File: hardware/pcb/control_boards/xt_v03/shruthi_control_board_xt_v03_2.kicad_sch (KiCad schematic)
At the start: 39 parts, among them IC4 4051N, IC5 4051N, IC6 4051N, IC7 4051N

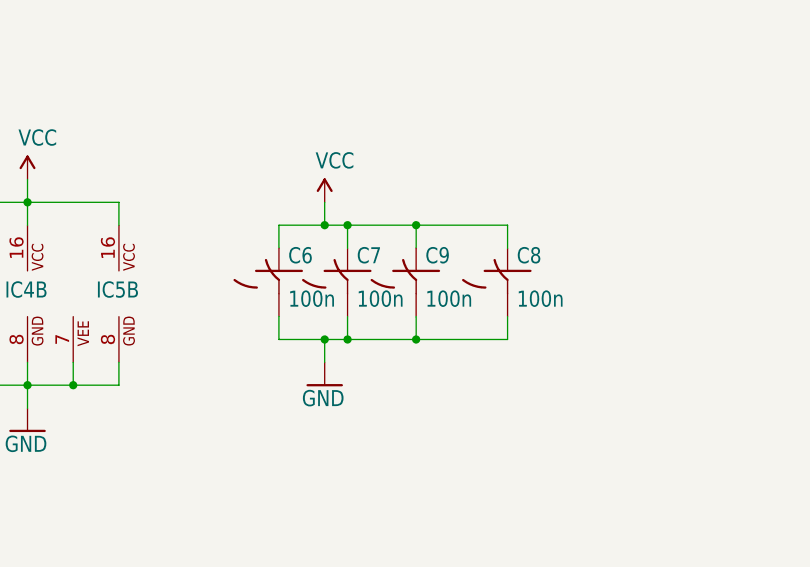
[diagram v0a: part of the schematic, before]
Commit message: update capacitors to use kicad symbols
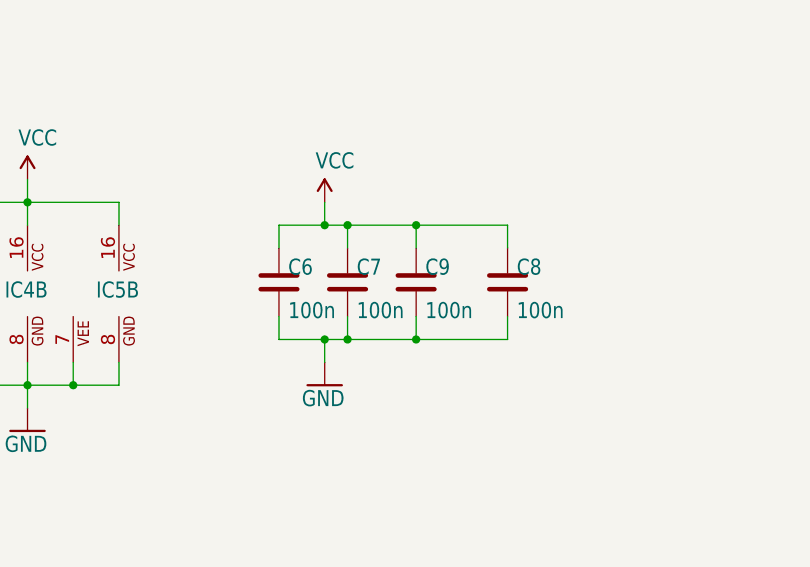
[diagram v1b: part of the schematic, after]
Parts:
- C6, C7, C8, C9: symbol shruthi_control_board_xt_v03-eagle-import:C-US025-024X044 -> Device:C
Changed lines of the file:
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@@
 	)
 	(symbol
-		(lib_id "shruthi_control_board_xt_v03-eagle-import:C-US025-024X044")
-		(at 142.24 223.52 0)
+		(lib_id "Device:C")
+		(at 142.24 224.79 0)
 		(unit 1)
 		(exclude_from_sim no)
@@
 		(dnp no)
 		(property "Reference" "C9"
-			(at 143.256 222.885 0)
+			(at 143.256 224.155 0)
 			(effects
 				(font
@@
 		)
 		(property "Value" "100n"
-			(at 143.256 227.711 0)
+			(at 143.256 228.981 0)
 			(effects
 				(font
@@
 		)
 		(property "Footprint" "shruthi_control_board_xt_v03:C025-024X044"
-			(at 142.24 223.52 0)
+			(at 143.2052 228.6 0)
 			(effects
 				(font
@@
 			)
 		)
-		(property "Datasheet" ""
-			(at 142.24 223.52 0)
+		(property "Datasheet" "~"
+			(at 142.24 224.79 0)
 			(effects
 				(font
@@
 			)
 		)
-		(property "Description" ""
-			(at 142.24 223.52 0)
+		(property "Description" "Unpolarized capacitor"
+			(at 142.24 224.79 0)
 			(effects
 				(font
@@
 	)
 	(symbol
-		(lib_id "shruthi_control_board_xt_v03-eagle-import:C-US025-024X044")
-		(at 134.62 223.52 0)
+		(lib_id "Device:C")
+		(at 134.62 224.79 0)
 		(unit 1)
 		(exclude_from_sim no)
@@
 		(dnp no)
 		(property "Reference" "C7"
-			(at 135.636 222.885 0)
+			(at 135.636 224.155 0)
 			(effects
 				(font
@@
 		)
 		(property "Value" "100n"
-			(at 135.636 227.711 0)
+			(at 135.636 228.981 0)
 			(effects
 				(font
@@
 		)
 		(property "Footprint" "shruthi_control_board_xt_v03:C025-024X044"
-			(at 134.62 223.52 0)
+			(at 135.5852 228.6 0)
 			(effects
 				(font
@@
 			)
 		)
-		(property "Datasheet" ""
-			(at 134.62 223.52 0)
+		(property "Datasheet" "~"
+			(at 134.62 224.79 0)
 			(effects
 				(font
@@
 			)
 		)
-		(property "Description" ""
-			(at 134.62 223.52 0)
+		(property "Description" "Unpolarized capacitor"
+			(at 134.62 224.79 0)
 			(effects
 				(font
@@
 	)
 	(symbol
-		(lib_id "shruthi_control_board_xt_v03-eagle-import:C-US025-024X044")
-		(at 127 223.52 0)
+		(lib_id "Device:C")
+		(at 127 224.79 0)
 		(unit 1)
 		(exclude_from_sim no)
@@
 		(dnp no)
 		(property "Reference" "C6"
-			(at 128.016 222.885 0)
+			(at 128.016 224.155 0)
 			(effects
 				(font
@@
 		)
 		(property "Value" "100n"
-			(at 128.016 227.711 0)
+			(at 128.016 228.981 0)
 			(effects
 				(font
@@
 		)
 		(property "Footprint" "shruthi_control_board_xt_v03:C025-024X044"
-			(at 127 223.52 0)
+			(at 127.9652 228.6 0)
 			(effects
 				(font
@@
 			)
 		)
-		(property "Datasheet" ""
-			(at 127 223.52 0)
+		(property "Datasheet" "~"
+			(at 127 224.79 0)
 			(effects
 				(font
@@
 			)
 		)
-		(property "Description" ""
-			(at 127 223.52 0)
+		(property "Description" "Unpolarized capacitor"
+			(at 127 224.79 0)
 			(effects
 				(font
@@
 	)
 	(symbol
-		(lib_id "shruthi_control_board_xt_v03-eagle-import:C-US025-024X044")
-		(at 152.4 223.52 0)
+		(lib_id "Device:C")
+		(at 152.4 224.79 0)
 		(unit 1)
 		(exclude_from_sim no)
@@
 		(dnp no)
 		(property "Reference" "C8"
-			(at 153.416 222.885 0)
+			(at 153.416 224.155 0)
 			(effects
 				(font
@@
 		)
 		(property "Value" "100n"
-			(at 153.416 227.711 0)
+			(at 153.416 228.981 0)
 			(effects
 				(font
@@
 		)
 		(property "Footprint" "shruthi_control_board_xt_v03:C025-024X044"
-			(at 152.4 223.52 0)
+			(at 153.3652 228.6 0)
 			(effects
 				(font
@@
 			)
 		)
-		(property "Datasheet" ""
-			(at 152.4 223.52 0)
+		(property "Datasheet" "~"
+			(at 152.4 224.79 0)
 			(effects
 				(font
@@
 			)
 		)
-		(property "Description" ""
-			(at 152.4 223.52 0)
+		(property "Description" "Unpolarized capacitor"
+			(at 152.4 224.79 0)
 			(effects
 				(font
